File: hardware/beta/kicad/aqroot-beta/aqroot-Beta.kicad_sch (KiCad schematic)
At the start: 0 parts

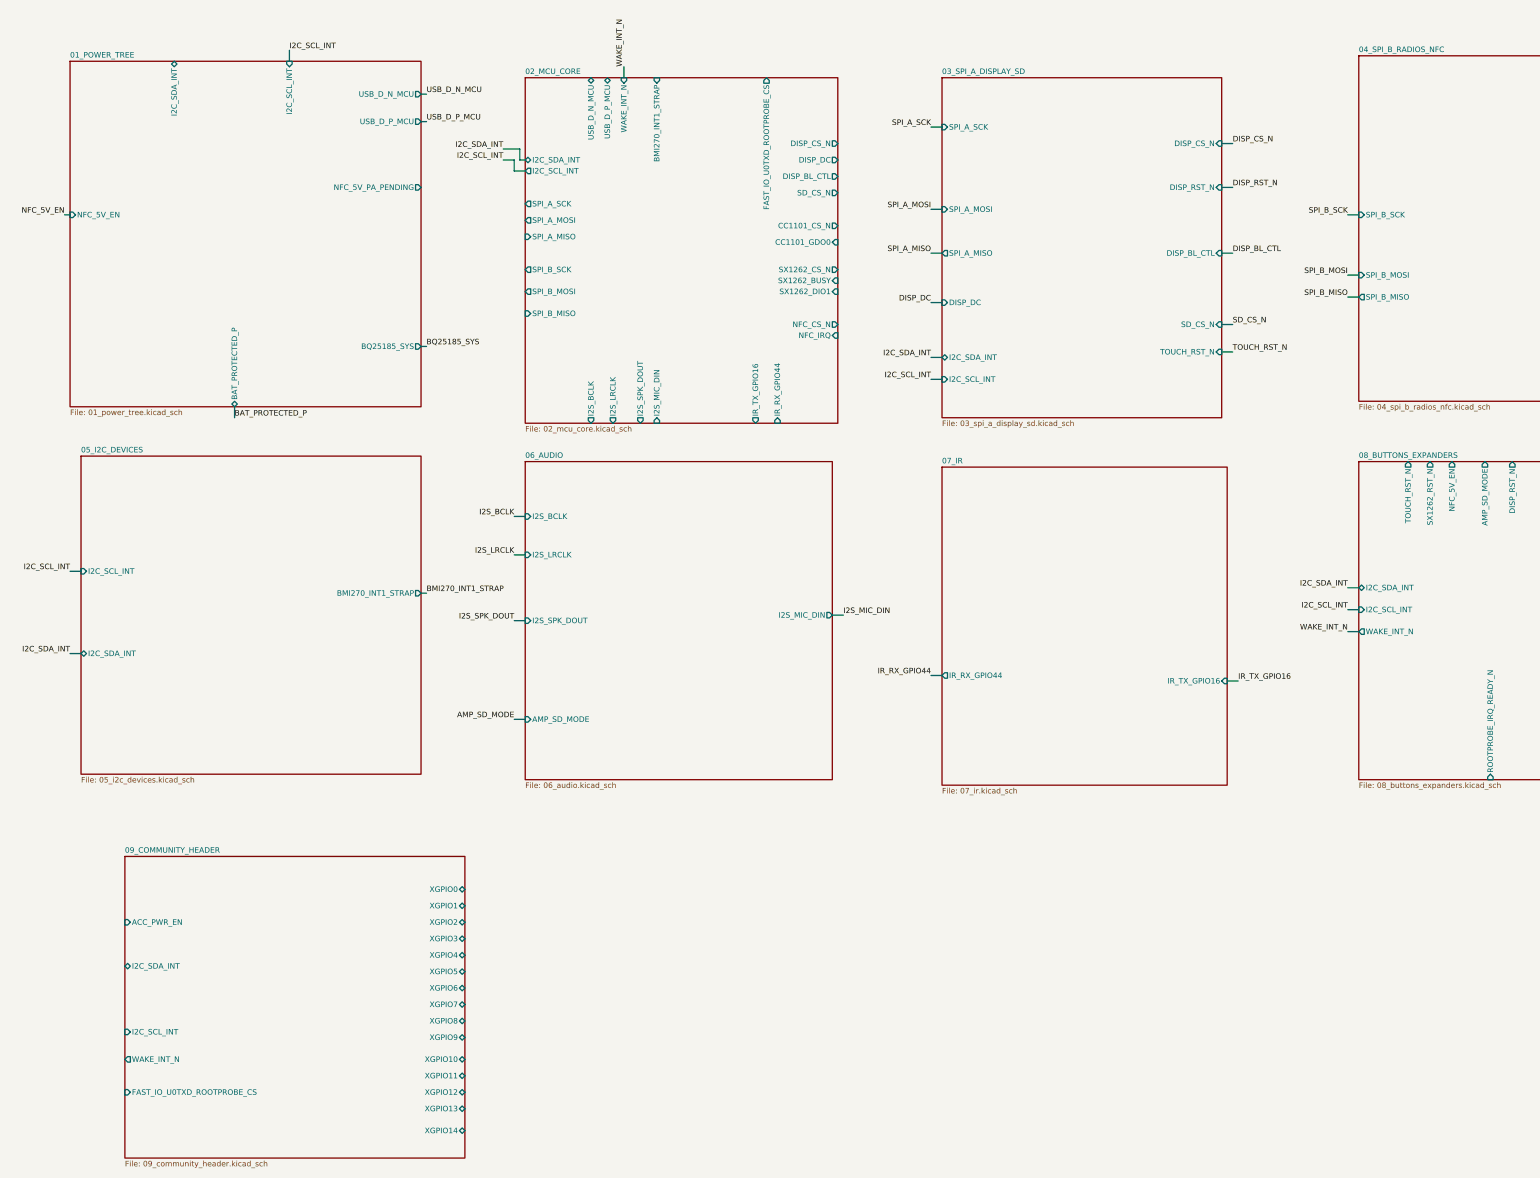
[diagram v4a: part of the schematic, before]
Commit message: Schematics: root connectivity pass for XGPIO, I2C_SDA_INT and NFC_5V_PA_PENDING
Work-in-progress checkpoint of the root-level connectivity pass. Verified with
kicad-cli netlist and ERC comparison against the previous commit.

Resolved:
- NFC_5V_PA_PENDING was split across two isolated sheet-local nets,
  /01_POWER_TREE/NFC_5V_PA_PENDING (C34.2 C35.1 R44.2 TP9.1 U13.6) and
  /04_SPI_B_RADIOS_NFC/NFC_5V_PA_PENDING (C19.1 alone). Promoted the local
  label in 04_spi_b_radios_nfc to a hierarchical input label, added the
  matching sheet pin on the root, and extended the wire to reach it. These
  now form a single root net /NFC_5V_PA_PENDING with all 6 nodes.
- I2C_SDA_INT: U14.8 was stranded on its own sheet-local net. It now joins
  the main /I2C_SDA_INT net (6 -> 7 nodes).
- ERC pin_not_connected: 77 -> 56 (21 pins newly connected).

Known incomplete, to be finished in a follow-up:
- 18 newly placed root labels are dangling because their wiring is not yet
  drawn: XGPIO0..XGPIO14, ACC_PWR_EN, FAST_IO_U0TXD_ROOTPROBE_CS, WAKE_INT_N.
  ERC label_dangling: 39 -> 57.
- REGRESSION: WAKE_INT_N lost U1.23 (MCU wake input). The root wire from
  (152.4, 24.13) to (152.4, 26.67) was removed, which disconnected the
  WAKE_INT_N label from the 02_MCU_CORE sheet pin at (152.4, 25.4). The net
  dropped from 4 nodes (R3.1 U1.23 U2.1 U3.1) to 3, and U1.23 is now an
  isolated /02_MCU_CORE/WAKE_INT_N. This must be reconnected before the
  netlist is used for layout.

Also clears the stale used_designators cache in the project file, a side
effect of the KiCad editing session.

No symbol, footprint, PCB or library-table changes.

Co-Authored-By: Claude Opus 5 <noreply@anthropic.com>
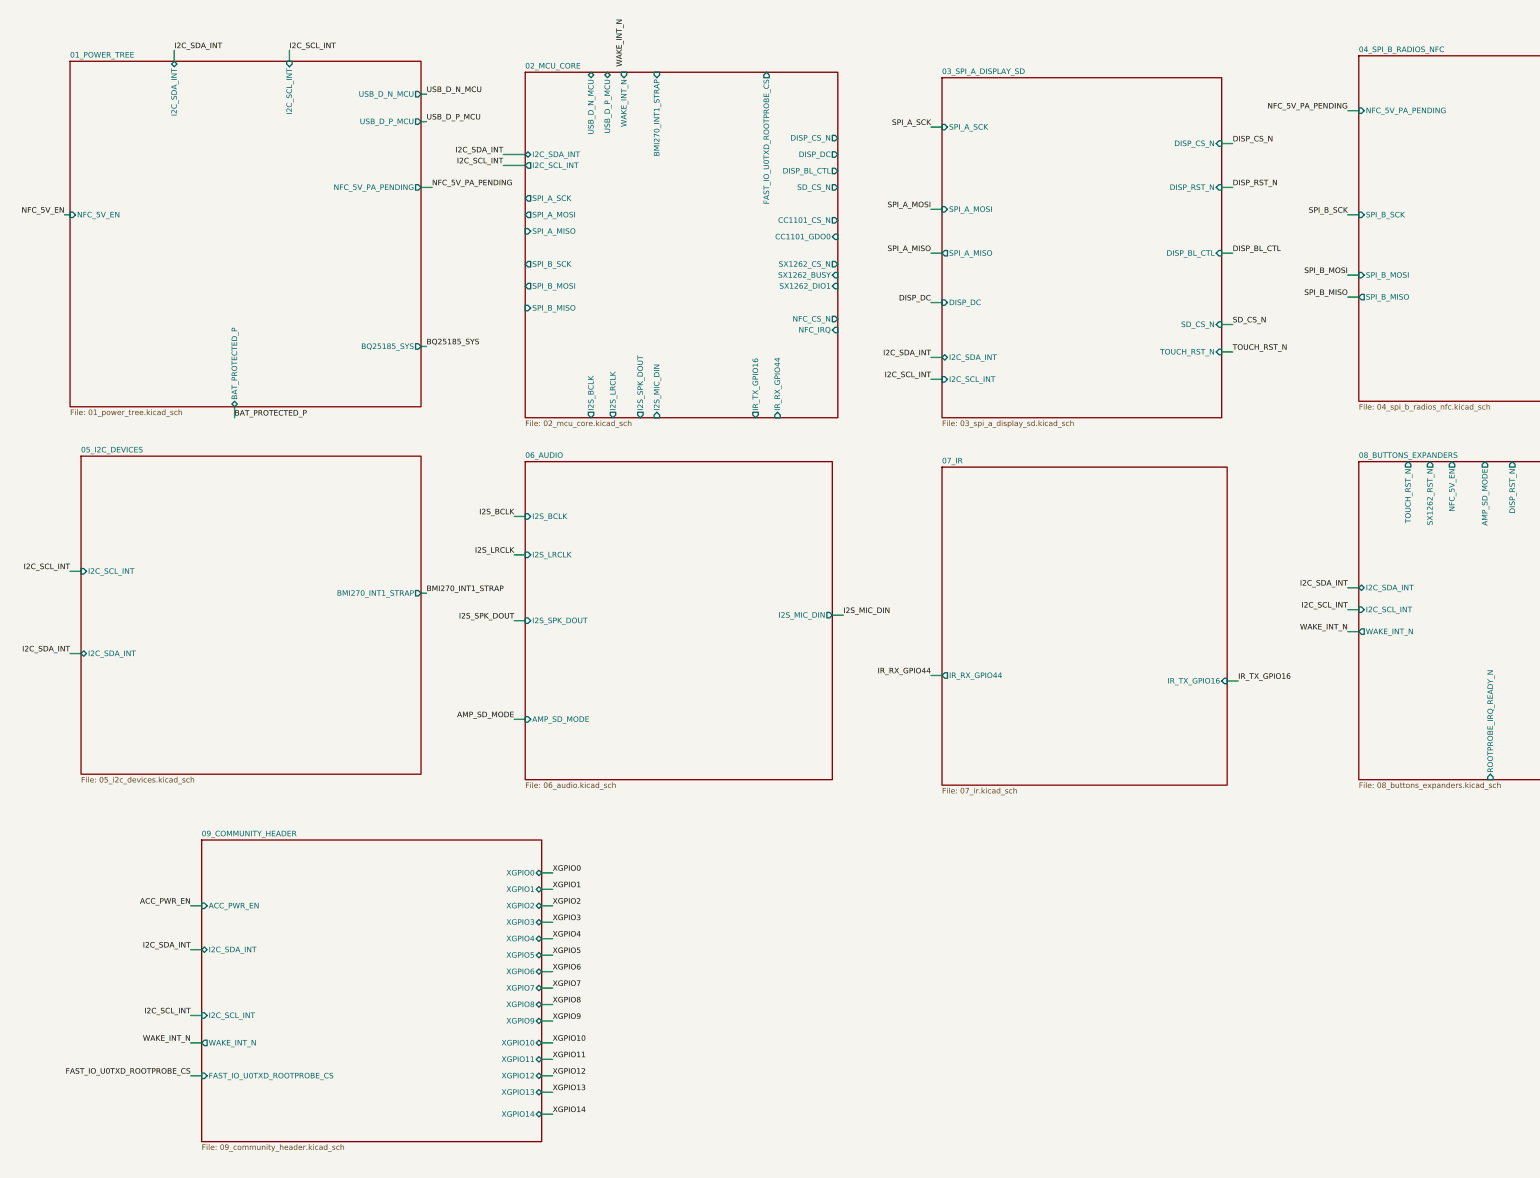
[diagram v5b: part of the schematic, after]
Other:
- sheet 04_SPI_B_RADIOS_NFC ports: added NFC_5V_PA_PENDING; removed none
